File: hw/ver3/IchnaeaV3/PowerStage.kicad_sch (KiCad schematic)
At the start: 80 parts, among them Q1 BSS138, U1 LTC7871, U12 LM1117MP-5.0, U13 LM1117MP-3.3, U8 AP66200FVBW-13

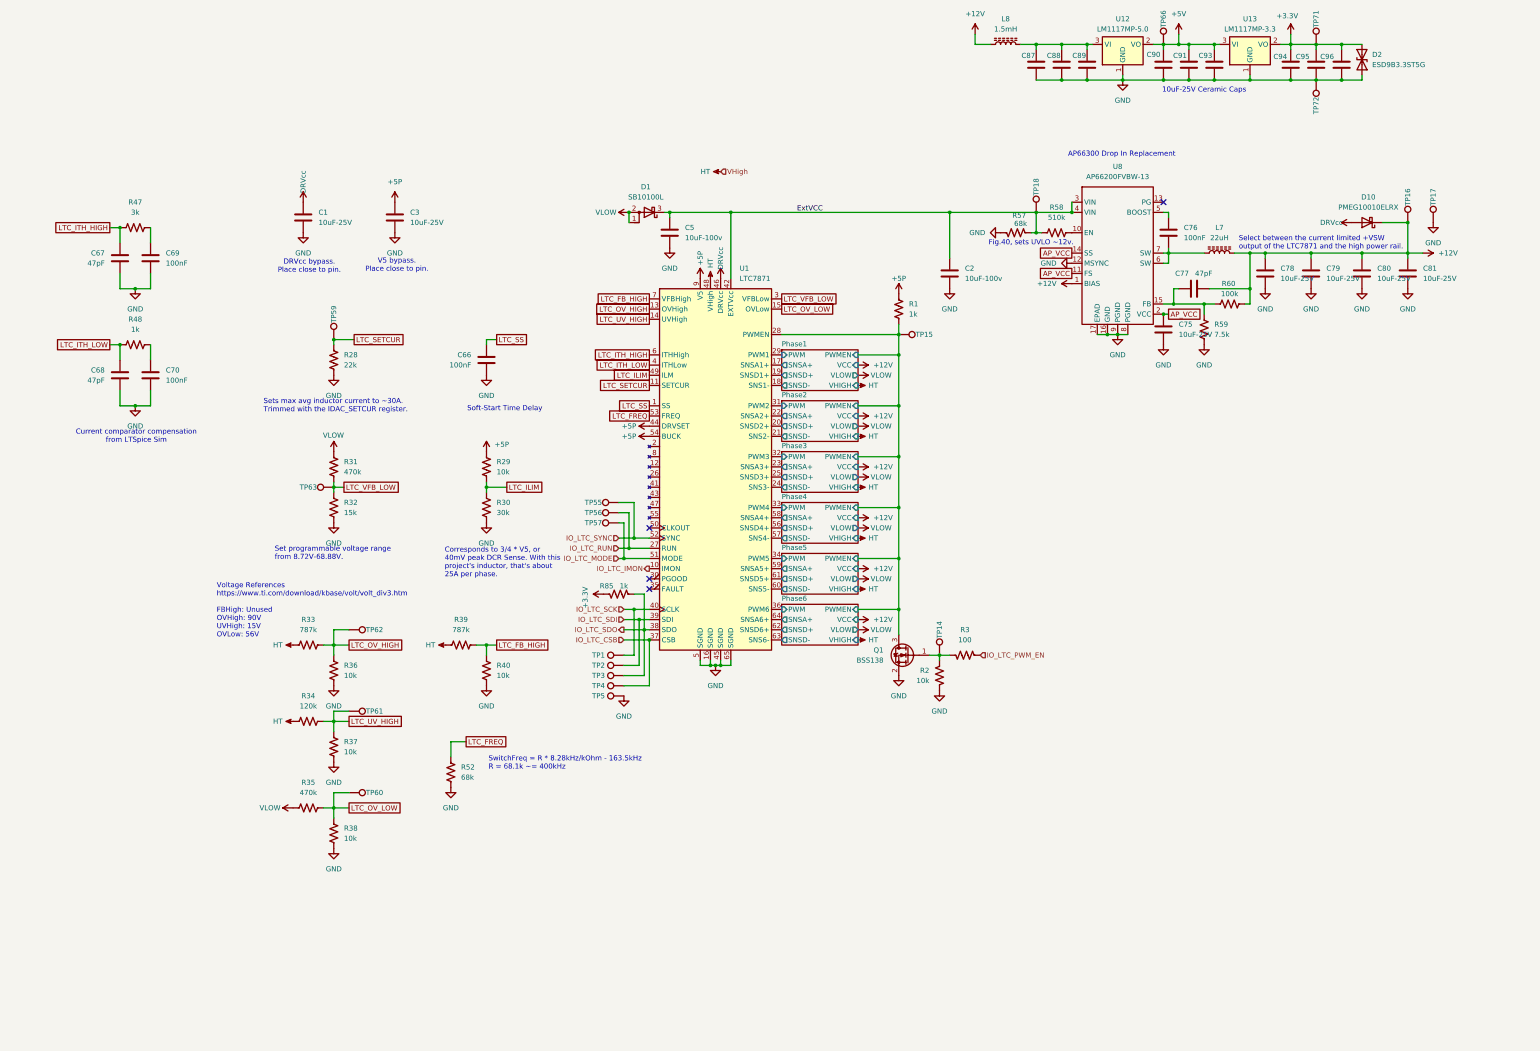
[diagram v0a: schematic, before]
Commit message: Experiment with a new power stage layout
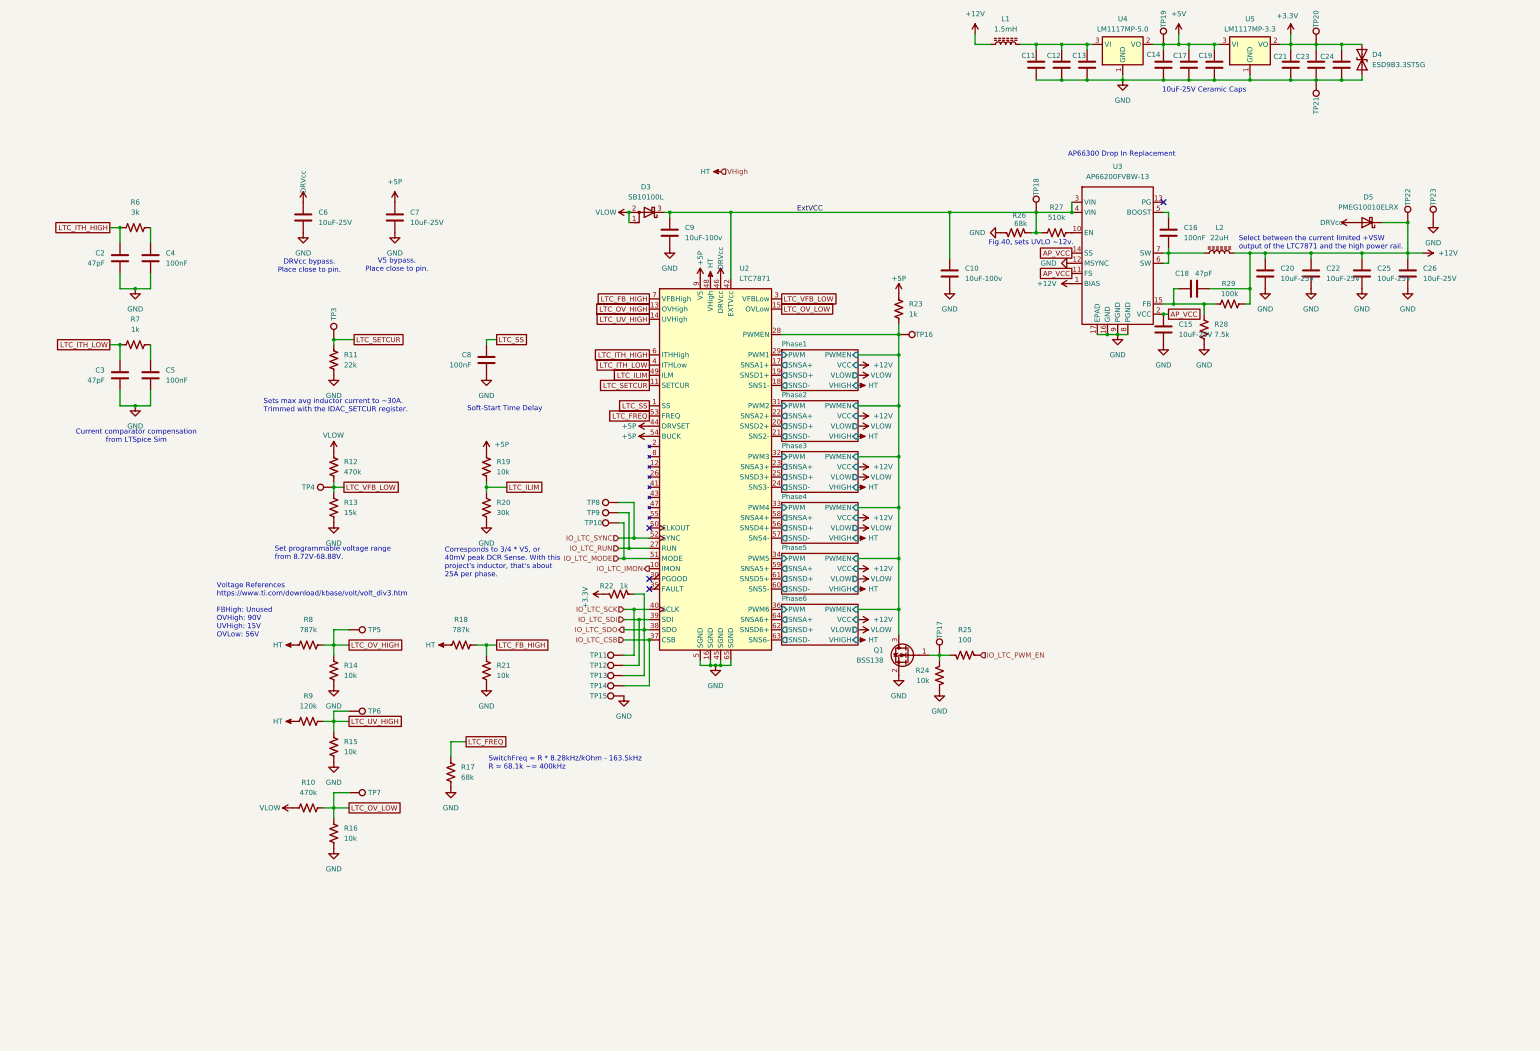
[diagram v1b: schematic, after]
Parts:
- renumbered C2 to C10, C87 to C11, C88 to C12, C89 to C13, C90 to C14, C75 to C15, C76 to C16, C91 to C17, C77 to C18, C93 to C19, C67 to C2, C78 to C20, C94 to C21, C79 to C22, C95 to C23, C96 to C24, C80 to C25, C81 to C26, C68 to C3, C69 to C4, C70 to C5, C1 to C6, C3 to C7, C66 to C8, C5 to C9, D1 to D3, D2 to D4, D10 to D5, L8 to L1, L7 to L2, R35 to R10, R28 to R11, R31 to R12, R32 to R13, R36 to R14, R37 to R15, R38 to R16, R52 to R17, R39 to R18, R29 to R19, R30 to R20, R40 to R21, R85 to R22, R1 to R23, R2 to R24, R3 to R25, R57 to R26, R58 to R27, R59 to R28, R60 to R29, R47 to R6, R48 to R7, R33 to R8, R34 to R9, TP57 to TP10, TP1 to TP11, TP2 to TP12, TP3 to TP13, TP4 to TP14, TP5 to TP15, TP15 to TP16, TP14 to TP17, TP66 to TP19, TP71 to TP20, TP72 to TP21, TP16 to TP22, TP17 to TP23, TP59 to TP3, TP63 to TP4, TP62 to TP5, TP61 to TP6, TP60 to TP7, TP55 to TP8, TP56 to TP9, U1 to U2, U8 to U3, U12 to U4, U13 to U5

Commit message: Swiftly correct the design issue.
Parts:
- removed L1: 1.5mH, Inductor_SMD:L_Changjiang_FNR6045S, symbol Device:L_Ferrite
- removed TP16, TP17, TP19, TP20, TP21, TP3: TestPoint, TestPoint:TestPoint_Pad_D1.0mm, symbol Connector:TestPoint
- R12: value 470k -> 348k; footprint Resistor_SMD:R_0805_2012Metric -> Resistor_SMD:R_0603_1608Metric; LCSC C17709 -> C23006
- R13: value 15k -> 12k; LCSC C22809 -> C22790
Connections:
- net +12V: now also C11.1, C12.1, C13.1, U4.3 (VI)
- net IO_LTC_IMON: no longer names the net of U2.10 (IMON)
- no-connect marks 4 -> 5
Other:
- note added: "SwitchFreq = R * 8.28kHz/kOhm R = 68.1k => 400kHz"
- note added: "TODO: Can I delete the 3.3v rail entirely?"
- note added: "TODO: Need to add high side load switch here. B2b N-Ch mos"
- note added: "Voltage Feedback Range: 13.73V - 58.27V Resolution: 0.3480V"
- note removed: "Set programmable voltage range from 8.72V-68.88V."
- note removed: "SwitchFreq = R * 8.28kHz/kOhm - 163.5kHz R = 68.1k ~= 400kHz"
- moved on the sheet: R12, R13, R17, R19, R20, TP4

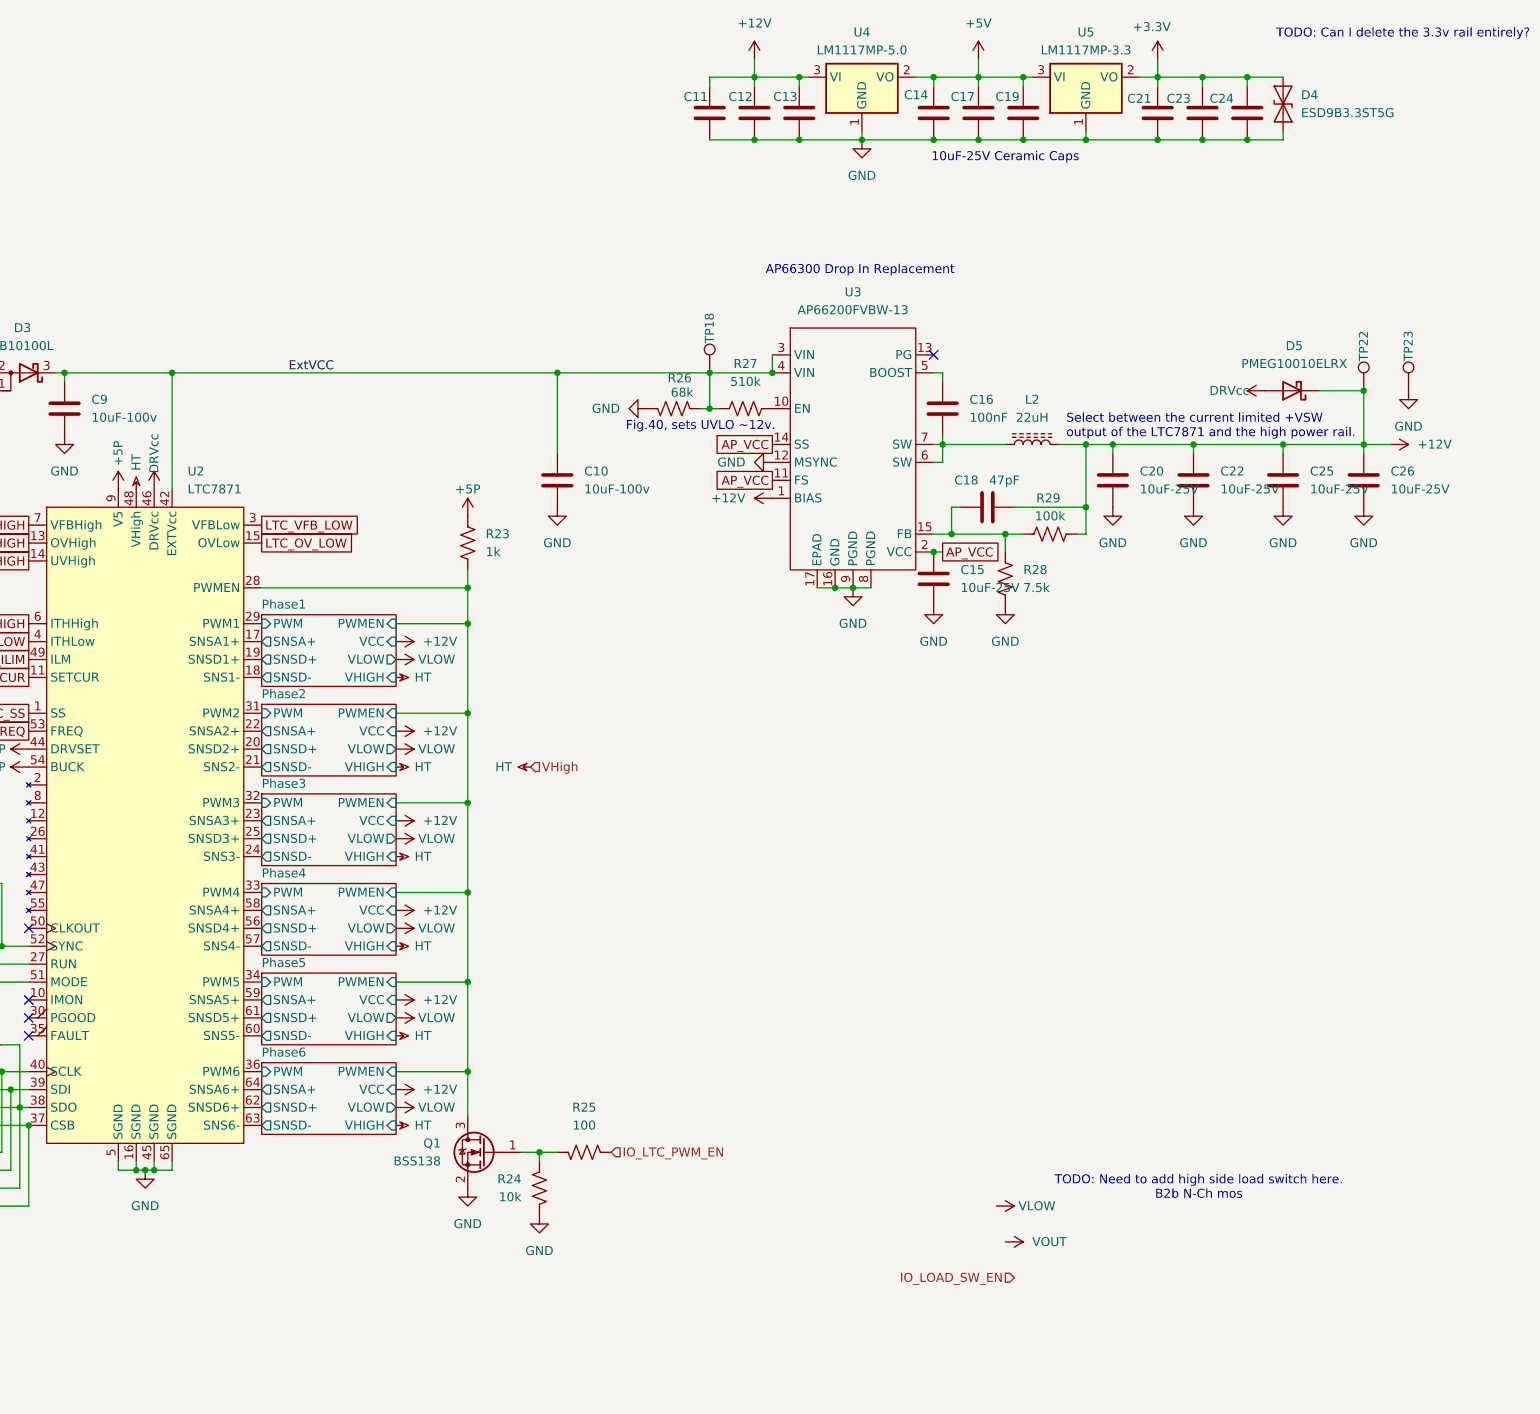
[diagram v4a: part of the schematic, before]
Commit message: Improve more of the power stage layout
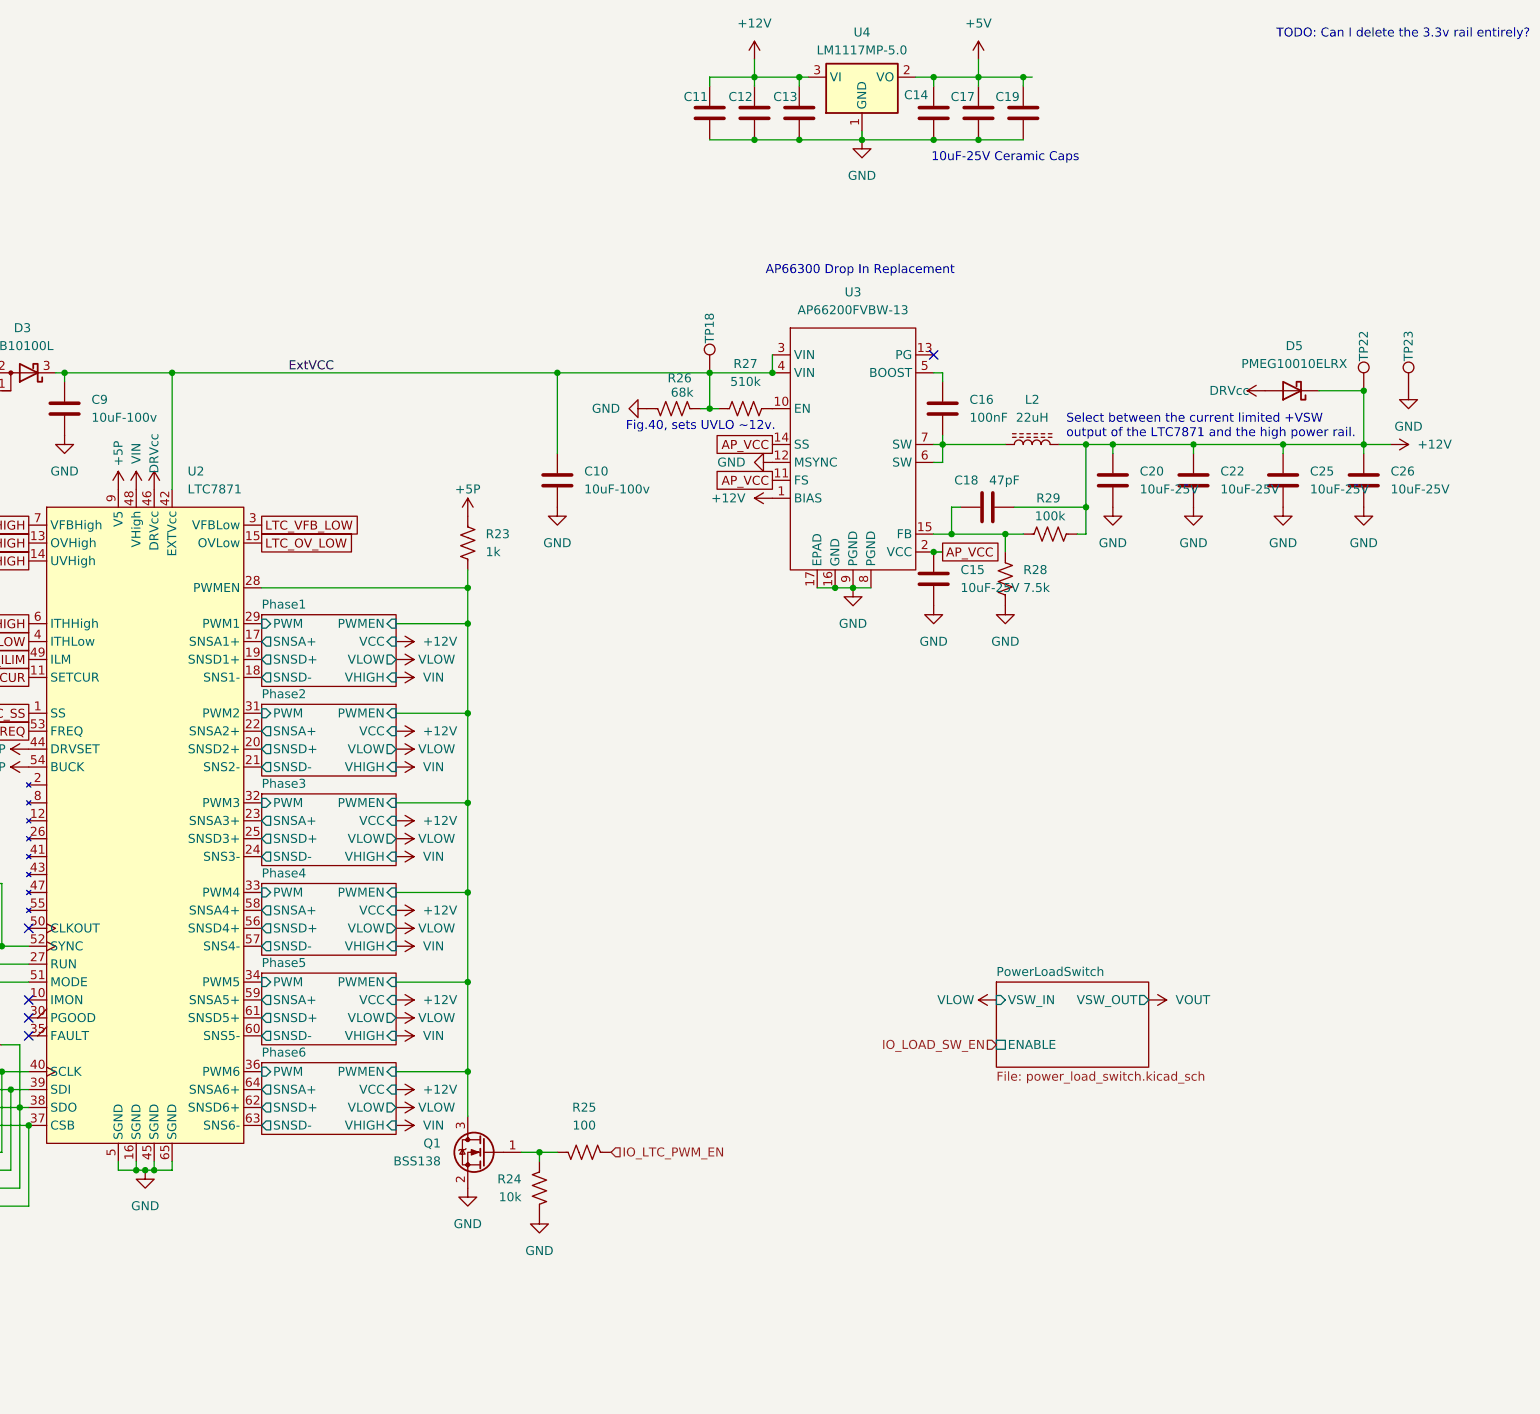
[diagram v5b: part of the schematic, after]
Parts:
- removed C21, C23, C24: 10uF-25V, Capacitor_SMD:C_0603_1608Metric, symbol Device:C
- removed D4: ESD9B3.3ST5G, Diode_SMD:D_SOD-923, symbol Diode:ESD9B3.3ST5G
- removed U5: LM1117MP-3.3, Package_TO_SOT_SMD:SOT-223-3_TabPin2, symbol Regulator_Linear:LM1117MP-3.3
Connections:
- net HT: no longer U2.48 (VHigh)
- new net VIN: U2.48 (VHigh)
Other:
- added sheet PowerLoadSwitch (power_load_switch.kicad_sch)
- note removed: "TODO: Need to add high side load switch here. B2b N-Ch mos"
